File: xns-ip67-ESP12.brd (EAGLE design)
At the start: 65.3 x 129.3 mm, 75 parts, among them J1 DCJ0202, J24 5V, X1 ESP-12E

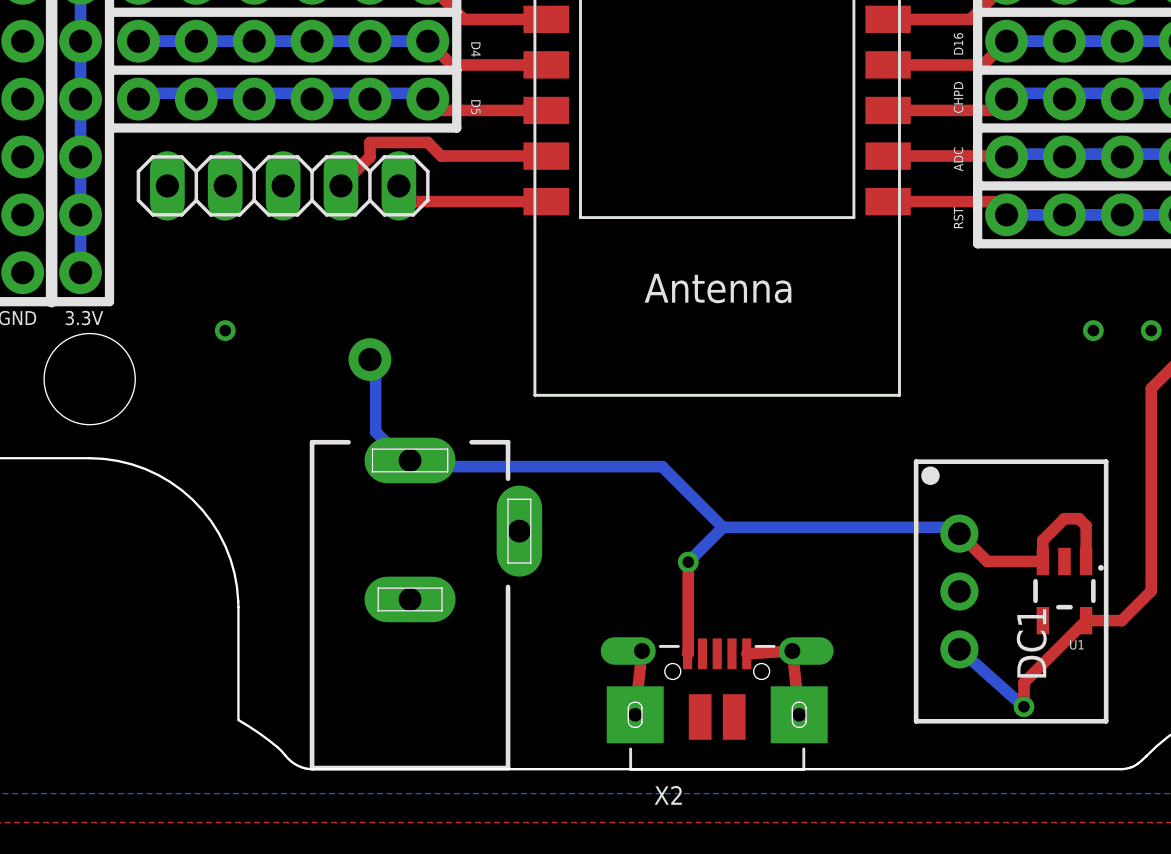
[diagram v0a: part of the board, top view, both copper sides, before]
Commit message: Board dimension changes
Adjusted to be edge to edge
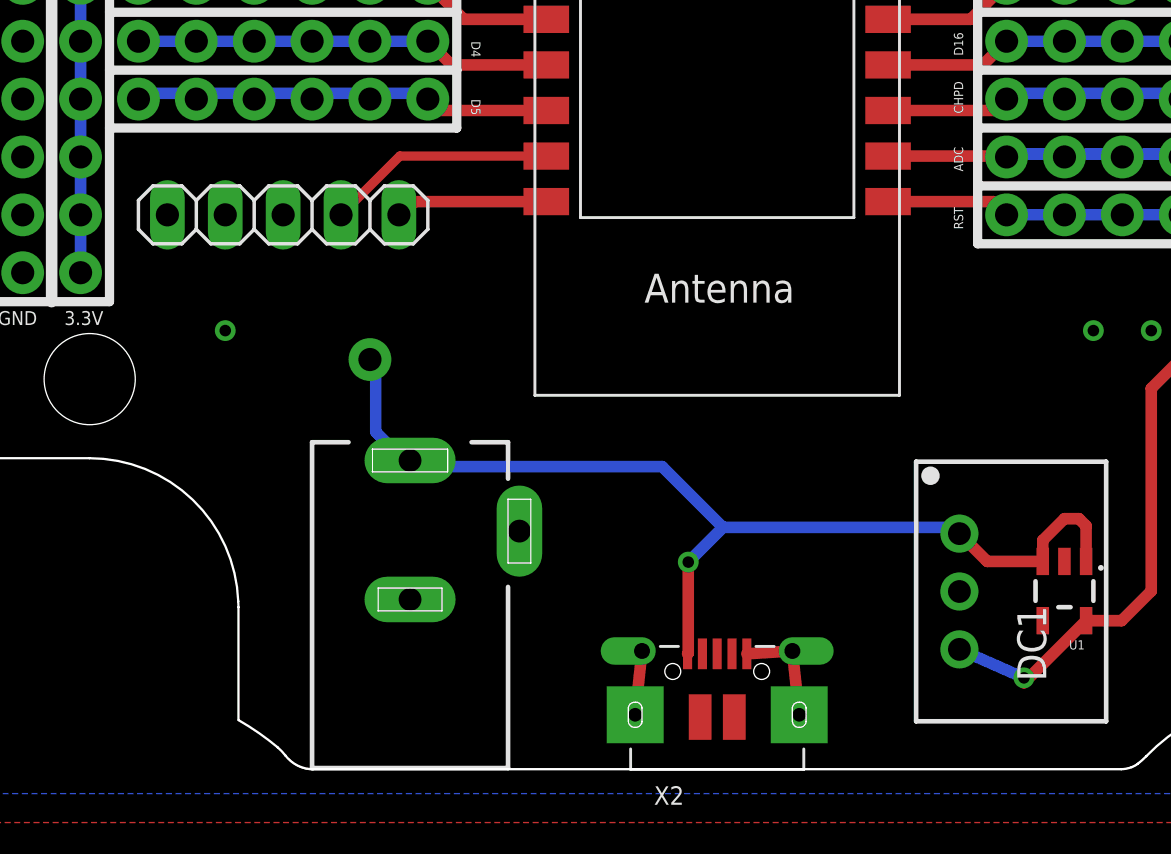
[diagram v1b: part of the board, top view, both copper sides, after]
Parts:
- moved JP37 1.27 mm to (24.1, 22.9)
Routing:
- net VDD: track 268.9 -> 267.4 mm
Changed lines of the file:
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@@
 <?xml version="1.0" encoding="utf-8"?>
 <!DOCTYPE eagle SYSTEM "eagle.dtd">
-<eagle version="7.7.0">
+<eagle version="8.0.0">
 <drawing>
 <settings>
@@
 <wire x1="62.23" y1="60.96" x2="64.77" y2="60.96" width="0.4064" layer="25"/>
 <wire x1="64.77" y1="60.96" x2="64.77" y2="63.5" width="0.4064" layer="25"/>
-<text x="26.035" y="20.955" size="1.016" layer="27">RX</text>
-<text x="17.78" y="20.955" size="1.016" layer="27">GND</text>
-<text x="28.575" y="20.955" size="1.016" layer="27">TX</text>
+<text x="26.035" y="19.685" size="1.016" layer="27">RX</text>
+<text x="17.78" y="19.685" size="1.016" layer="27">GND</text>
+<text x="28.575" y="19.685" size="1.016" layer="27">TX</text>
 <text x="37.465" y="123.19" size="1.778" layer="25">xnsense.no</text>
 <text x="32.385" y="119.38" size="1.778" layer="25">xns ip67-ESP12 rev 1</text>
@@
 <attribute name="VALUE" x="44.45" y="59.055" size="1.27" layer="27"/>
 </element>
-<element name="JP37" library="pinhead" package="1X05" value="" x="24.13" y="24.13" smashed="yes">
-<attribute name="VALUE" x="17.78" y="20.955" size="1.27" layer="27"/>
+<element name="JP37" library="pinhead" package="1X05" value="" x="24.13" y="22.86" smashed="yes">
+<attribute name="VALUE" x="17.78" y="19.685" size="1.27" layer="27"/>
 </element>
 <element name="J2" library="SparkFun-Connectors" package="1X06_NO_SILK" value="" x="55.88" y="38.1" smashed="yes">
@@
 <wire x1="71.247" y1="25.146" x2="71.247" y2="22.86" width="0.508" layer="16"/>
 <wire x1="71.247" y1="25.146" x2="71.12" y2="25.4" width="0.508" layer="16"/>
-<wire x1="56.642" y1="1.27" x2="53.81" y2="3.79" width="0.508" layer="16"/>
+<wire x1="56.642" y1="2.54" x2="53.81" y2="3.79" width="0.508" layer="16"/>
 <wire x1="70.866" y1="20.574" x2="71.12" y2="20.32" width="0.508" layer="16"/>
 <wire x1="71.247" y1="20.574" x2="71.247" y2="22.86" width="0.508" layer="16"/>
@@
 <wire x1="51.816" y1="47.371" x2="51.435" y2="46.99" width="0.508" layer="16"/>
 <via x="51.435" y="46.99" extent="1-16" drill="0.508"/>
-<via x="56.642" y="1.27" extent="1-16" drill="0.508"/>
-<wire x1="56.642" y1="1.27" x2="56.642" y2="2.3219" width="0.508" layer="1"/>
+<via x="56.642" y="2.54" extent="1-16" drill="0.508"/>
+<wire x1="56.642" y1="2.54" x2="56.642" y2="2.3219" width="0.508" layer="1"/>
 <wire x1="56.642" y1="2.3219" x2="59.37" y2="5.0499" width="0.508" layer="1"/>
 <wire x1="59.37" y1="5.0499" x2="60.9299" y2="5.0499" width="0.508" layer="1"/>
@@
 <contactref element="X1" pad="16"/>
 <wire x1="35.68" y1="23.44" x2="29.9" y2="23.44" width="0.508" layer="1"/>
-<wire x1="29.9" y1="23.44" x2="29.21" y2="24.13" width="0.508" layer="1"/>
+<wire x1="29.9" y1="23.44" x2="29.21" y2="22.86" width="0.508" layer="1"/>
 </signal>
 <signal name="N$13">
 <contactref element="JP37" pad="4"/>
 <contactref element="X1" pad="15"/>
-<wire x1="35.68" y1="25.44" x2="31.075" y2="25.44" width="0.508" layer="1"/>
-<wire x1="31.075" y1="25.44" x2="30.48" y2="26.035" width="0.508" layer="1"/>
-<wire x1="30.48" y1="26.035" x2="27.94" y2="26.035" width="0.508" layer="1"/>
-<wire x1="27.94" y1="26.035" x2="27.94" y2="25.4" width="0.508" layer="1"/>
-<wire x1="27.94" y1="25.4" x2="26.67" y2="24.13" width="0.508" layer="1"/>
+<wire x1="35.68" y1="25.44" x2="29.25" y2="25.44" width="0.4064" layer="1"/>
+<wire x1="29.25" y1="25.44" x2="26.67" y2="22.86" width="0.4064" layer="1"/>
 </signal>
 <signal name="N$1">

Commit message: New board for Temp
New board for Temp logging with A7, Power lines is routed
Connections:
- net VCC: now also JP37.2
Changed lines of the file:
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@@
 <?xml version="1.0" encoding="utf-8"?>
 <!DOCTYPE eagle SYSTEM "eagle.dtd">
-<eagle version="8.0.0">
+<eagle version="8.0.2">
 <drawing>
 <settings>
@@
 <element name="J1" library="con-jack" package="DCJ0202" value="DCJ0202" x="29.7" y="8.98" smashed="yes">
 <attribute name="MF" value="" x="29.7" y="8.98" size="1.778" layer="27" display="off"/>
+<attribute name="MPN" value="" x="29.7" y="8.98" size="1.778" layer="27" display="off"/>
+<attribute name="OC_FARNELL" value="unknown" x="29.7" y="8.98" size="1.778" layer="27" display="off"/>
 <attribute name="OC_NEWARK" value="unknown" x="29.7" y="8.98" size="1.778" layer="27" display="off"/>
-<attribute name="OC_FARNELL" value="unknown" x="29.7" y="8.98" size="1.778" layer="27" display="off"/>
-<attribute name="MPN" value="" x="29.7" y="8.98" size="1.778" layer="27" display="off"/>
 <attribute name="VALUE" x="24.62" y="3.9" size="1.27" layer="27" rot="R90"/>
 </element>
@@
 <wire x1="57.47" y1="7.6501" x2="57.47" y2="8.575" width="0.508" layer="1"/>
 <wire x1="57.47" y1="8.575" x2="58.42" y2="9.525" width="0.508" layer="1"/>
+<contactref element="JP37" pad="2"/>
+<wire x1="27.94" y1="16.51" x2="21.59" y2="22.86" width="0" layer="19" extent="1-1"/>
 </signal>
 <signal name="VDD">
